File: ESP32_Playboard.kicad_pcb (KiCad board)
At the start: 4 copper layers, 58 parts, among them J1 USB_B_Micro, J2 TF_PUSH, Q1 Q_NPN_BEC, Q2 Q_NPN_BEC, Q3 Q_NPN_BEC, SW1 SW_SPST, SW2 SW_SPST, U1 AMS1117-3.3, U2 USBLC6-2SC6, U3 CH340G, U4 ZD25Q64BS, U5 ESP32-D0WD-V3, U6 MPU-6050, U7 SHT30-DIS, Y1 12MHz, Y2 40MHz

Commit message: Worked more on PCB layout
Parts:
- removed R3: 0, Resistor_SMD:R_0603_1608Metric
- moved D1 109.7 mm to (116.8, 75.1), turned to 90 degrees
- moved C11 88.2 mm to (116.0, 71.6)
- moved C15 81.8 mm to (95.2, 69.3)
- moved D2 80.7 mm to (87.6, 79.5)
- moved R4 80.0 mm to (112.5, 71.4), turned to 90 degrees
- moved U7 79.6 mm to (130.6, 30.0)
- moved C22 78.8 mm to (105.9, 68.6)
- moved C23 75.4 mm to (98.8, 72.9)
- moved Q1 74.9 mm to (87.3, 75.6)
- moved J1 72.1 mm to (89.9, 18.0), turned to 180 degrees
- moved R5 71.9 mm to (87.4, 81.2), turned to 180 degrees
- moved C14 69.8 mm to (95.5, 65.8)
- moved U1 66.4 mm to (105.4, 21.3)
- moved C24 64.8 mm to (127.7, 29.8), turned to 90 degrees
- moved U3 59.3 mm to (88.9, 30.0), turned to 90 degrees
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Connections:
- net /OSC_N renamed /OSC-
- C7 pad 1: Net-(C7-Pad1) -> /OSC+
- U5 pad 45: /OSC_P -> /OSC+
- Y2 pad 1: Net-(C7-Pad1) -> /OSC+
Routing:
- net Net-(U5-Pad2): track 0.00 -> 46.9 mm
- net /REG_3V3: track 20.3 -> 0.03 mm
- net /CH_DTR: track 0.00 -> 14.1 mm
- net Net-(J1-Pad6): track 0.00 -> 11.5 mm
- net /CH_RTS: track 0.00 -> 9.72 mm
- net /USB_D-: track 0.00 -> 7.87 mm
- net /USB_D+: track 0.00 -> 7.87 mm
- net /USB_5V: track 0.00 -> 7.26 mm
- net Net-(C21-Pad1): track 7.09 -> 0.00 mm
- net Net-(C12-Pad2): track 6.67 -> 0.00 mm
- net /CH_XI: track 0.00 -> 6.48 mm
- net Net-(C7-Pad1): track 6.45 -> 0.00 mm
- net /CH_XO: track 0.00 -> 6.42 mm
- net /OSC_P: track 5.58 -> 0.00 mm
- net /OSC-: track 11.3 -> 6.25 mm
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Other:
- net class Default: trace_width 0.25 -> 0.254
- board text added: "BOOT"
- board text added: "RESET"

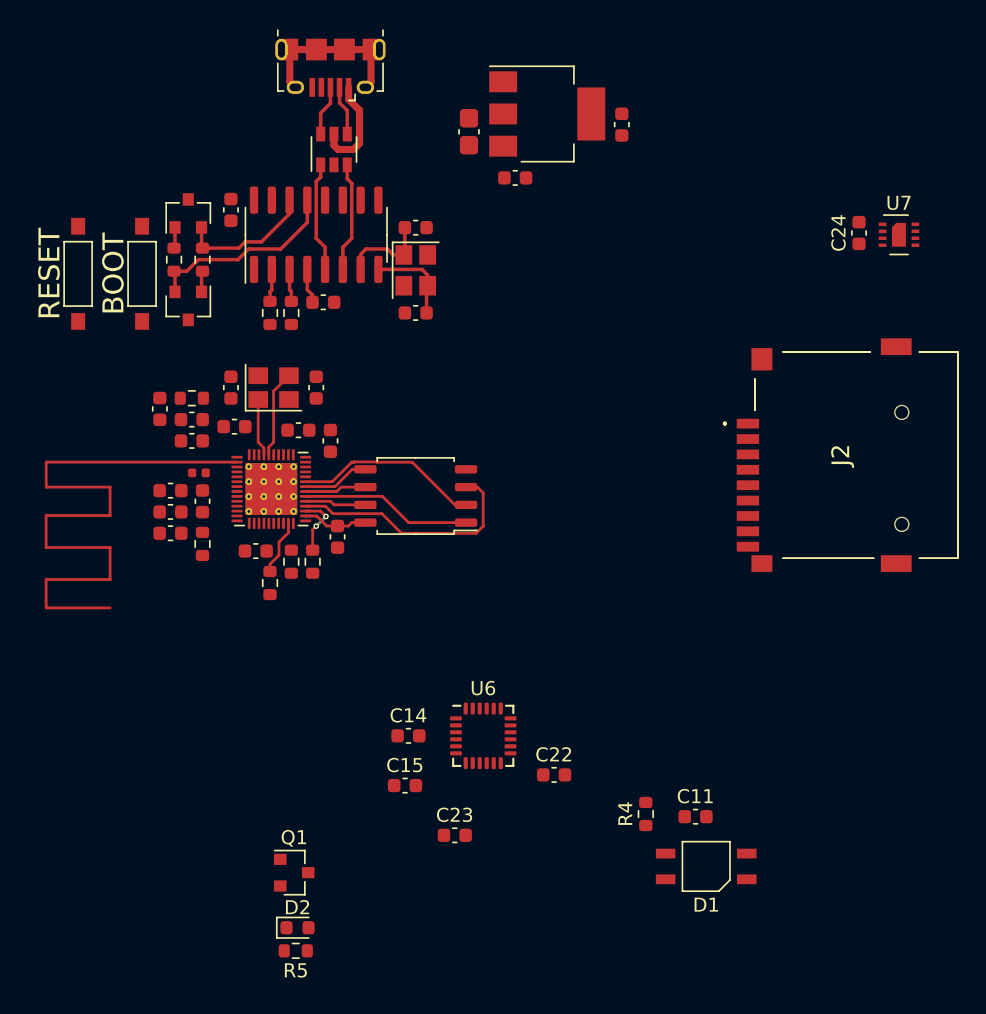
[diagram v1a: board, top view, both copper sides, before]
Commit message: Finished majority of PCB design
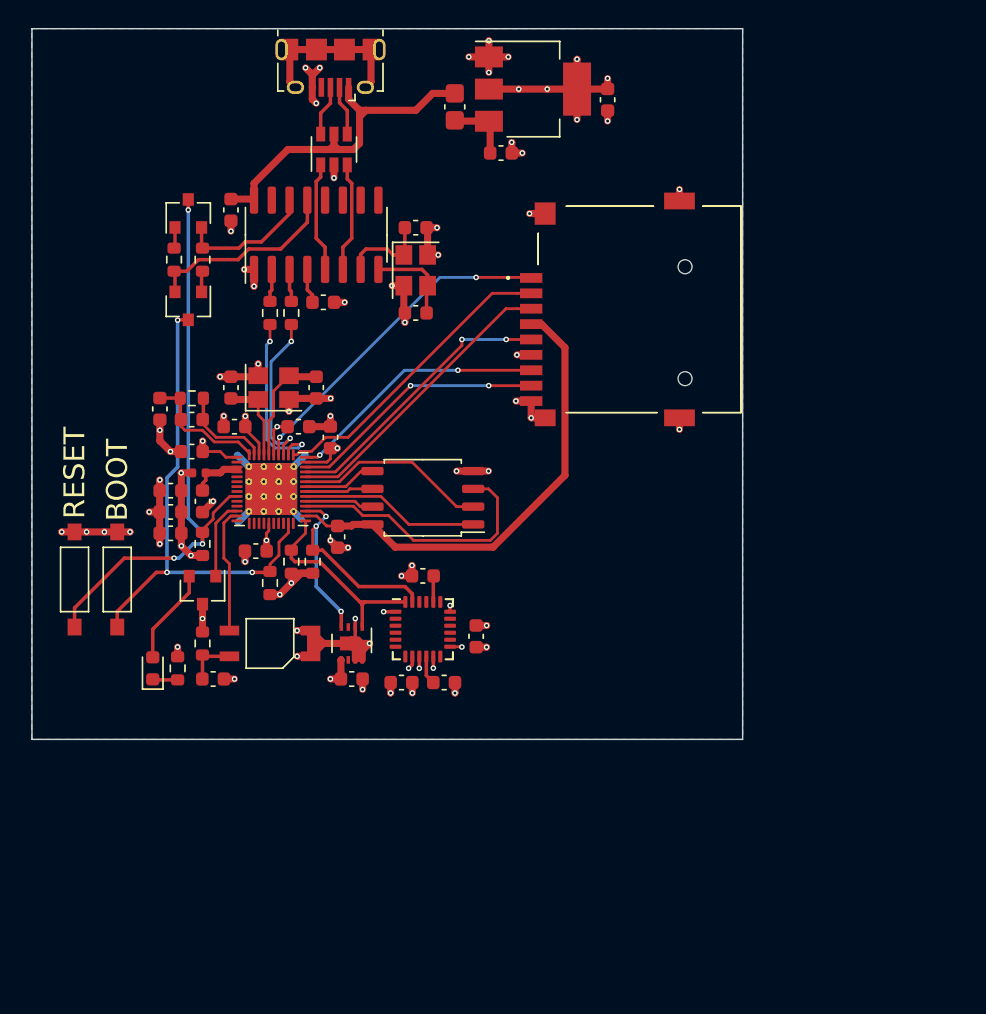
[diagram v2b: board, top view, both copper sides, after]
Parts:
- moved U7 48.8 mm to (91.4, 59.2), turned to 270 degrees
- moved C24 48.3 mm to (91.4, 61.7), turned to 0 degrees
- moved C11 35.9 mm to (81.5, 61.7)
- moved D1 35.0 mm to (85.6, 59.2)
- moved R4 34.0 mm to (80.8, 59.2)
- moved SW2 21.9 mm to (74.7, 54.6)
- moved R5 21.9 mm to (79.0, 61.0), turned to 270 degrees
- moved SW1 21.8 mm to (71.6, 54.6), turned to 180 degrees
- moved D2 21.2 mm to (77.2, 61.0), turned to 90 degrees
- moved Q1 21.2 mm to (80.8, 55.4), turned to 270 degrees
- moved C23 18.7 mm to (96.5, 54.4), turned to 180 degrees
- moved J2 18.7 mm to (112.0, 35.3)
- moved C15 11.8 mm to (100.3, 58.7), turned to 90 degrees
- moved C22 10.3 mm to (98.0, 62.0)
- moved U6 8.76 mm to (96.5, 58.2)
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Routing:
- net GND: track 0.00 -> 115.6 mm, vias 0 -> 62
- net /REG_3V3: track 0.03 -> 49.8 mm, vias 0 -> 21
- net Net-(U5-Pad2): track 46.9 -> 0.00 mm
- net /ESP_EN: track 0.00 -> 42.2 mm, vias 0 -> 3
- net /GPIO0: track 3.99 -> 36.3 mm, vias 0 -> 3
- net /VDD_SDIO: track 4.67 -> 33.9 mm
- net /SPI3_D2: track 0.00 -> 24.1 mm, vias 0 -> 2
- net /SPI3_D3: track 0.00 -> 21.8 mm
- net /SPI3_CS0: track 0.00 -> 21.1 mm
- net /SPI3_CLK: track 0.00 -> 20.3 mm, vias 0 -> 2
- net /USB_5V: track 7.26 -> 26.0 mm
- net /SPI3_D0: track 0.00 -> 18.7 mm, vias 0 -> 2
- net /SPI3_D1: track 0.00 -> 18.5 mm, vias 0 -> 2
- net /I2C0_SCL: track 4.42 -> 21.4 mm, vias 2 -> 3
- net /I2C0_SDA: track 0.00 -> 14.6 mm
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- added copper zone on Power.Cu, net /REG_3V3
- added copper zone on B.Cu, net GND
- added copper zone on GND.Cu, net GND
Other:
- board outline added: 50.8 x 50.8 mm

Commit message: Finished PCB design
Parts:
- added C14: 2pF, Capacitor_SMD:C_0603_1608Metric, F.Cu at (75.2, 42.4)
- added C15: 2.7pF, Capacitor_SMD:C_0603_1608Metric, F.Cu at (76.7, 45.5)
- added L1: 2.7mH, Inductor_SMD:L_0603_1608Metric, F.Cu at (75.2, 45.5)
- added U5: PCB_ANT, PlayboardLib:ESPRESSIF_ESP32_MIFA_2.4GHz_Right, F.Cu at (74.2, 44.5)
- renumbered C14 to C16, C15 to C17, C16 to C18, C17 to C19, C18 to C20, C19 to C21, C20 to C22, C21 to C23, C22 to C24, C23 to C25, C24 to C26, C25 to C27, C26 to C28, L1 to L2, R11 to R10, R12 to R11, R4 to R3, R5 to R4, R6 to R5, R7 to R6, R8 to R7, R9 to R8, R10 to R9, U5 to U6, U6 to U7, U7 to U8
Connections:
- U6 pad 2: Net-(U5-Pad2) -> /ANT
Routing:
- net /ANT: track 0.00 -> 8.07 mm
- net Net-(C14-Pad1): track 0.00 -> 2.51 mm
- net GND: track 115.6 -> 117.1 mm, vias 62 -> 65

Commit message: Finished basic PCB layout (no routing)
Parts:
- removed the C10 at (83.1, 43.7)
- removed the C12 at (77.7, 42.4)
- removed the C13 at (80.0, 43.2)
- removed the C14 at (75.2, 42.4)
- removed C15: 2.7pF, Capacitor_SMD:C_0603_1608Metric
- removed C18, C19, C22, C23, C28: 100nF, Capacitor_SMD:C_0603_1608Metric
- removed C20: 10uF, Capacitor_SMD:C_0603_1608Metric
- removed C21, C27: 1uF, Capacitor_SMD:C_0603_1608Metric
- removed the C7 at (82.8, 40.9)
- removed L1: 2.7mH, Inductor_SMD:L_0603_1608Metric
- removed L2: 2nH, Inductor_SMD:L_0402_1005Metric
- removed the R6 at (80.8, 52.1)
- removed the R9 at (85.6, 54.9)
- removed the U5 at (74.2, 44.5)
- removed the U6 at (85.7, 48.1)
- removed Y2: 40MHz, Crystal:Crystal_SMD_3225-4Pin_3.2x2.5mm
- C8: value 20pF -> 22uF
- C9: value 100pF -> 100nF
- D1: footprint PlayboardLib:LED_SMD-4 -> PlayboardLib:LED-SMD-4
- R5: value 20K (5%) -> 10k
- U4: value ZD25Q64BS -> ESP32-WROVER-I; footprint Package_SO:SOP-8_5.28x5.23mm_P1.27mm -> PlayboardLib:XCVR_ESP32-WROVER-I
- moved C6 38.9 mm to (70.9, 20.8), turned to 90 degrees
- moved R5 28.5 mm to (108.5, 43.2), turned to 270 degrees
- moved U1 28.0 mm to (76.5, 21.6), turned to 180 degrees
- moved D2 24.8 mm to (70.4, 37.1), turned to 270 degrees
- moved R4 24.8 mm to (72.1, 37.1), turned to 90 degrees
- moved C5 24.5 mm to (78.7, 16.8), turned to 180 degrees
- moved SW2 24.3 mm to (77.5, 30.5)
- moved SW1 24.1 mm to (71.6, 30.5)
- moved C9 23.4 mm to (111.0, 43.9), turned to 180 degrees
- moved C14 22.8 mm to (70.9, 51.8)
- moved C11 22.4 mm to (93.5, 37.3), turned to 180 degrees
- moved C8 22.1 mm to (111.0, 42.2), turned to 180 degrees
- moved C12 22.1 mm to (97.3, 39.9), turned to 90 degrees
- moved U6 20.9 mm to (71.1, 54.4), turned to 180 degrees
- moved C10 19.2 mm to (97.3, 42.9), turned to 270 degrees
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- renumbered C16 to C10, C17 to C11, C24 to C12, C25 to C13, C26 to C14, C11 to C7, R7 to R6, R8 to R7, R11 to R8, R10 to R9, U7 to U5, U8 to U6
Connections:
- C8 pad 1: /OSC- -> GND
- C8 pad 2: GND -> /REG_3V3
- C9 pad 1: /REG_3V3 -> GND
- C9 pad 2: GND -> /REG_3V3
- D2 pad 1: Net-(D2-Pad1) -> GND
- J2 pad 4: /VDD_SDIO -> /REG_3V3
- Q1 pad 2: Net-(D2-Pad2) -> Net-(Q1-Pad2)
- Q2 pad 3: /ESP_EN -> /RESET
- R4 pad 1: GND -> Net-(D2-Pad2)
- R4 pad 2: Net-(D2-Pad1) -> Net-(Q1-Pad2)
- R5 pad 1: Net-(C12-Pad2) -> /REG_3V3
- R5 pad 2: Net-(C13-Pad2) -> /RESET
- SW1 pad 1: GND -> /RESET
- SW1 pad 2: /ESP_EN -> GND
- U4 pad 1: /FLASH_CMD -> GND
- U4 pad 2: /FLASH_D1 -> /REG_3V3
- U4 pad 3: /FLASH_D2 -> /RESET
- U4 pad 4: GND -> Net-(U4-Pad4)
- U4 pad 5: /FLASH_D0 -> Net-(U4-Pad5)
- U4 pad 6: /FLASH_CLK -> /IR_RECV
- U4 pad 7: /FLASH_D3 -> Net-(U4-Pad7)
- U4 pad 8: /VDD_SDIO -> /IR_SEND
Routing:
- net GND: track 117.1 -> 0.00 mm, vias 65 -> 0
- net /REG_3V3: track 49.8 -> 0.00 mm, vias 21 -> 0
- net /ESP_EN: track 42.2 -> 0.00 mm, vias 3 -> 0
- net /GPIO0: track 36.3 -> 0.00 mm, vias 3 -> 0
- net /VDD_SDIO: track 33.9 -> 0.00 mm
- net /USB_5V: track 26.0 -> 0.00 mm
- net /SPI3_D2: track 24.1 -> 0.00 mm, vias 2 -> 0
- net /SPI3_D3: track 21.8 -> 0.00 mm
- net /I2C0_SCL: track 21.4 -> 0.00 mm, vias 3 -> 0
- net /SPI3_CS0: track 21.1 -> 0.00 mm
- net /SPI3_CLK: track 20.3 -> 0.00 mm, vias 2 -> 0
- net /FLASH_D2: track 20.3 -> 0.00 mm
- net /SPI3_D0: track 18.7 -> 0.00 mm, vias 2 -> 0
- net /SPI3_D1: track 18.5 -> 0.00 mm, vias 2 -> 0
- net /I2C0_SDA: track 14.6 -> 0.00 mm
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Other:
- outline, holes or cut-outs redrawn

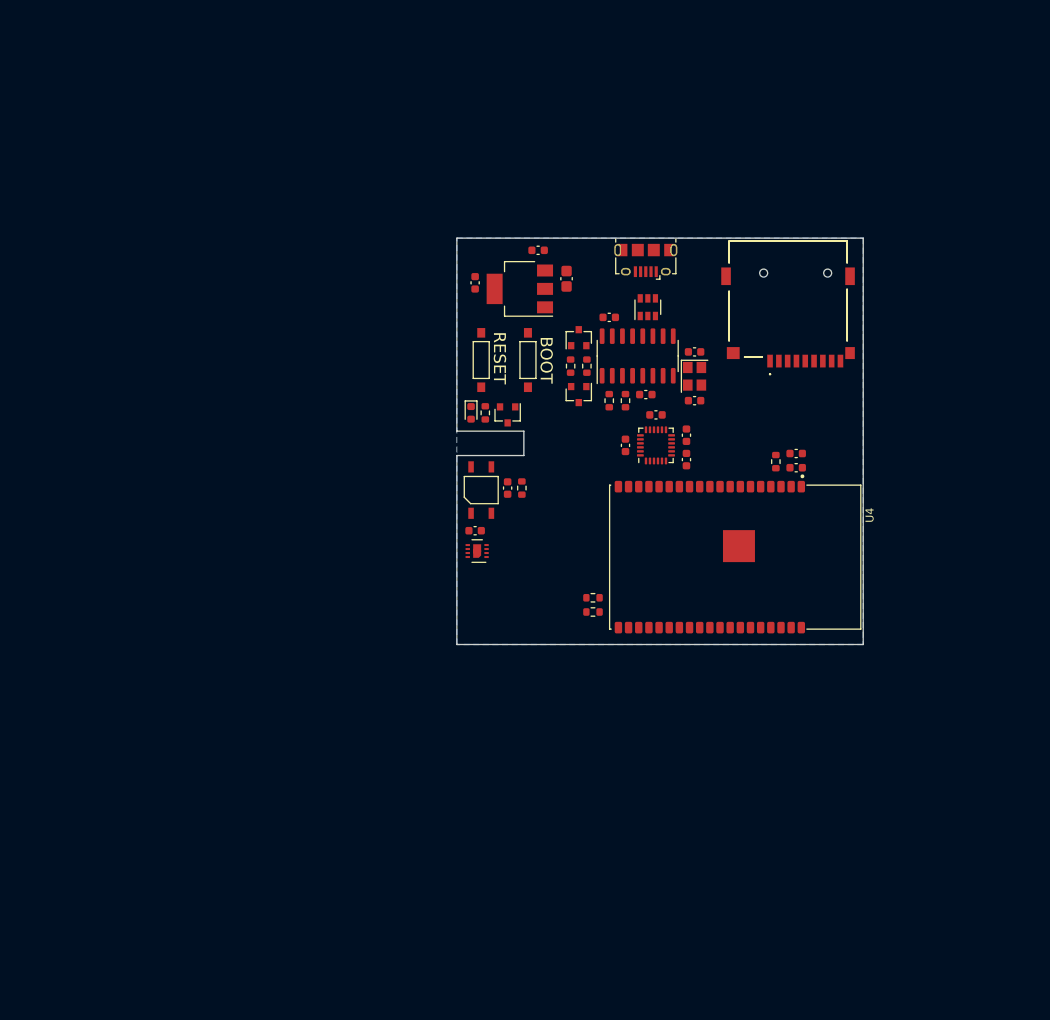
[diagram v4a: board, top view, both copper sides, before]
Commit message: Finished PCB layout
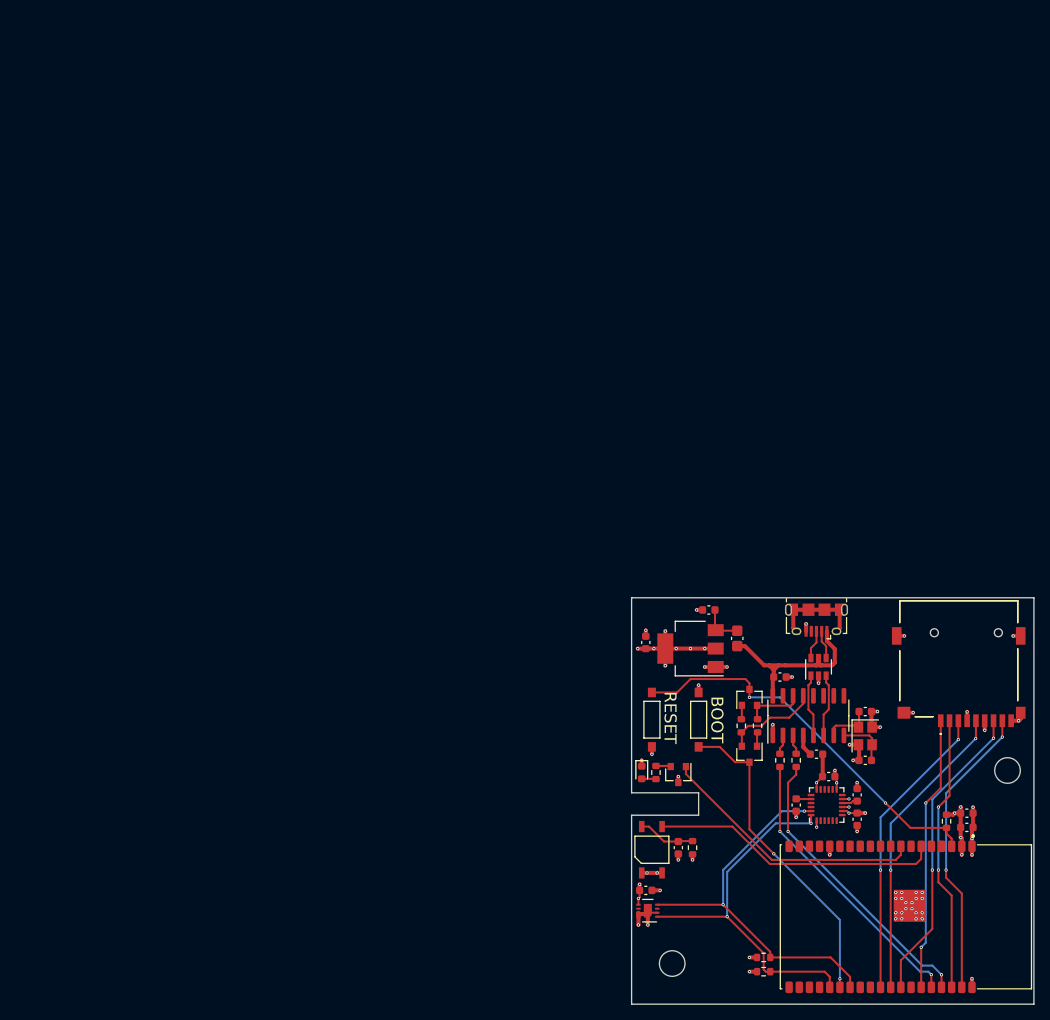
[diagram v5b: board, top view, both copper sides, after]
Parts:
- added H2: MountingHole, MountingHole:MountingHole_3.2mm_M3, F.Cu at (137.4, 81.8)
- added H3: MountingHole, MountingHole:MountingHole_3.2mm_M3, F.Cu at (95.5, 105.9)
- moved C9 50.1 mm to (115.1, 82.5)
- moved Q2 49.8 mm to (105.2, 72.6)
- moved R5 49.8 mm to (129.8, 88.1)
- moved J2 49.8 mm to (131.3, 67.8)
- moved Q3 49.8 mm to (105.2, 79.8)
- moved U1 49.8 mm to (97.8, 66.5)
- moved C11 49.8 mm to (132.3, 88.9)
- moved D1 49.8 mm to (93.0, 91.7)
- moved F1 49.8 mm to (103.6, 65.3)
- moved Q1 49.8 mm to (96.3, 82.3)
- moved R7 49.8 mm to (106.9, 105.2)
- moved U3 49.8 mm to (112.5, 74.9)
- moved C1 49.8 mm to (109.0, 70.1)
- moved C10 49.8 mm to (132.3, 87.1)
- moved C12 49.8 mm to (118.6, 84.8)
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- renumbered C8 to C10, C9 to C11, C10 to C8, C11 to C9, U5 to U4, U4 to U5
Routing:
- net GND: track 0.00 -> 52.5 mm, vias 0 -> 58
- net /RESET: track 0.00 -> 48.8 mm, vias 0 -> 2
- net /I2C0_SCL: track 0.00 -> 47.9 mm, vias 0 -> 2
- net /I2C0_SDA: track 0.00 -> 46.8 mm, vias 0 -> 2
- net /GPIO0: track 0.00 -> 40.0 mm, vias 0 -> 2
- net /SPI3_D0: track 0.00 -> 38.1 mm, vias 0 -> 2
- net /SPI3_CLK: track 0.00 -> 37.7 mm, vias 0 -> 2
- net /SPI3_CS0: track 0.00 -> 37.3 mm, vias 0 -> 2
- net /SPI3_D1: track 0.00 -> 37.0 mm, vias 0 -> 2
- net /ESP_TX: track 0.00 -> 36.7 mm, vias 0 -> 2
- net /IR_RECV: track 0.00 -> 36.2 mm
- net /ESP_RX: track 0.00 -> 36.0 mm, vias 0 -> 2
- net /SPI3_D3: track 0.00 -> 34.6 mm, vias 0 -> 2
- net /REG_3V3: track 0.00 -> 34.4 mm, vias 0 -> 22
- net /SPI3_D2: track 0.00 -> 34.3 mm, vias 0 -> 2
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- removed copper zone on B.Cu, net GND
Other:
- board size 50.8 x 50.8 mm -> 50.3 x 50.8 mm
